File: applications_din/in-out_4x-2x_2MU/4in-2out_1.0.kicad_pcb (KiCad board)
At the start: 2 copper layers, 86.5 x 33 mm, 62 parts, among them IC1 ULN2803, J1 Con_CTRL, J2 Con_IO, J5 Con_230V, K1 HFE20-1/24-1HSD-L2, K2 HFE20-1/24-1HSD-L2, U1 74HC595, U2 74HC165, X9 W237-102

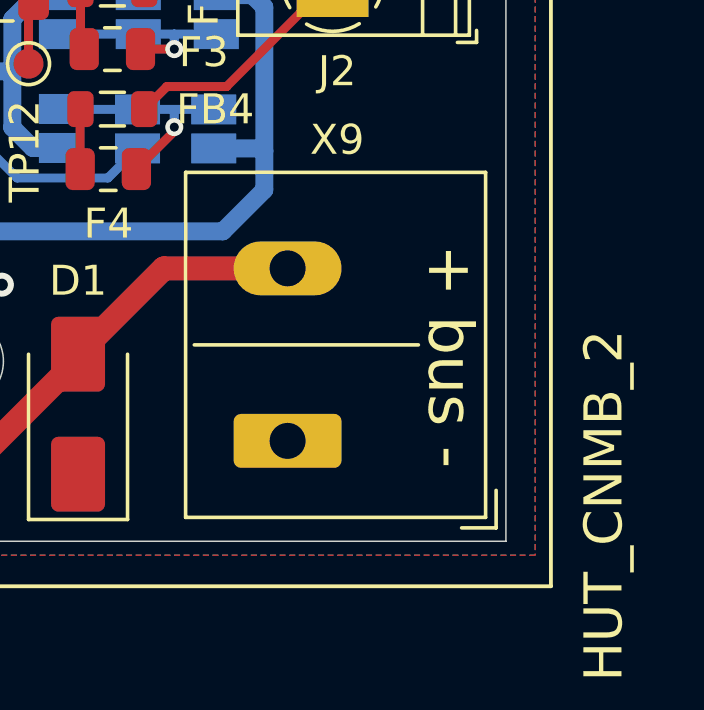
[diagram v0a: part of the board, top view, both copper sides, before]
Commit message: fixup! properly rename 4in-2out application & top projects
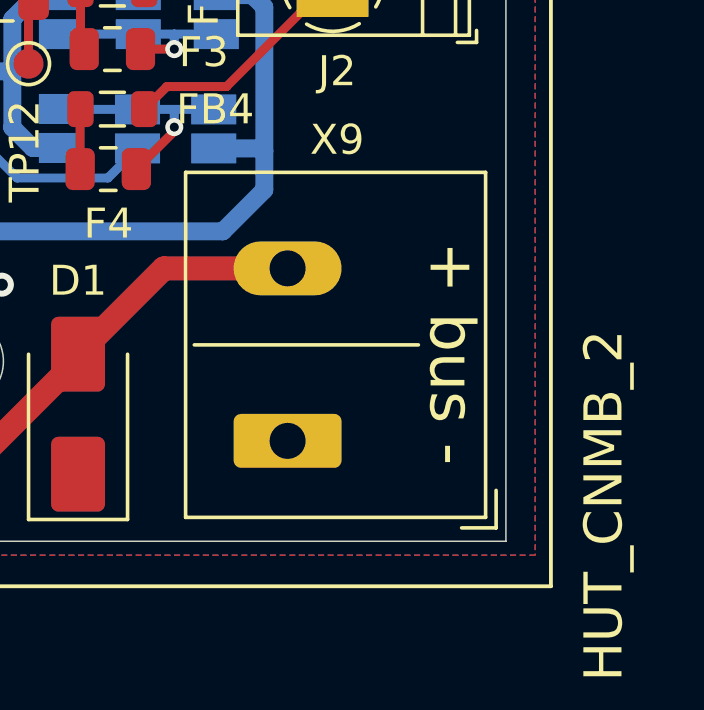
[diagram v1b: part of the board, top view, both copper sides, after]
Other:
- board text removed: "- bus +"
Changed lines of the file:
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@@
 			)
 		)
-		(property "Footprint" ""
+		(property "Footprint" "selfbus:HUT_CNMB_2"
 			(at 0 0 90)
 			(unlocked yes)
@@
 		)
 	)
-	(gr_text "- bus +"
-		(at 189.145 62.738 270)
+	(gr_text "+ bus -"
+		(at 191.008 62.484 90)
 		(layer "B.SilkS")
 		(effects
@@
 	)
 	(gr_text "+ bus -"
-		(at 190.1952 62.5856 -90)
+		(at 190.246 62.484 -90)
 		(layer "F.SilkS")
 		(effects

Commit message: update in-out_4x-2x_2MU - final for now
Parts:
- removed X9: W237-102, selfbus:W243-211_1x02_P5.75
- added J4: EIB_WAGO_243-211, selfbus:W243-211_1x02_P5.75, F.Cu at (184.7, 65.4)
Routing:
- net unconnected-(K2-Pad12): track 7.50 -> 0.00 mm
- net unconnected-(K1-Pad12): track 7.50 -> 0.00 mm
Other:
- board text added: "www.selfbus.org Kombiaktor 4in 2out v1.0"
- board text removed: "www.selfbus.org Kombiaktor 4in 2out v2.0"

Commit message: update all stuff
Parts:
- J1: footprint Connector_PinHeader_2.54mm:PinHeader_1x09_P2.54mm_Vertical -> Connector_Molex:Molex_KK-254_AE-6410-10A_1x10_P2.54mm_Vertical
- U2: renamed from IC1; value ULN2803 -> ULN2803A
- moved TP7 2.29 mm to (173.2, 59.6)
- moved R1 2.13 mm to (170.2, 60.2)
- moved TP9 1.99 mm to (152.1, 61.3)
- moved SJ1 1.88 mm to (167.4, 60.7)
- moved TP8 1.50 mm to (157.4, 61.3)
- moved TP3 1.41 mm to (160.0, 61.3)
- moved TP1 1.40 mm to (149.5, 61.3)
- moved C1 0.38 mm to (162.9, 57.8)
- moved J1 0.15 mm to (149.6, 66.0), turned to 0 degrees
- renumbered U2 to U3
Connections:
- J1 pad 1: VBUS -> GND
- J1 pad 2: GND -> VBUS
- J1 pad 3: +3V3 -> GND
- J1 pad 4: /PWM -> +3V3
- J1 pad 5: /MOSI -> /PWM
- J1 pad 6: /SSEL -> /MOSI
- J1 pad 7: /MISO -> /SSEL
- J1 pad 8: /SCK -> /MISO
- J1 pad 9: /EIB_DC -> /SCK
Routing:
- net /PWM: track 3.42 -> 5.70 mm
- net VDD: track 77.9 -> 79.8 mm
- net /SCK: track 45.7 -> 47.5 mm
- net +3V3: track 102.5 -> 101.3 mm, vias 6 -> 7
- net /MISO: track 30.9 -> 32.1 mm
- net /SSEL: track 42.1 -> 43.2 mm
- net /EIB_DC: track 11.1 -> 12.2 mm
- net GND: track 1.78 -> 2.81 mm
- net /MOSI: track 24.8 -> 25.8 mm
- net VBUS: track 43.0 -> 43.7 mm
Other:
- board text added: "- bus +"
